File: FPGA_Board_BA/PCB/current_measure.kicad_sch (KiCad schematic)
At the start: 1 part, among them U2 AMC0300D

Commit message: some changes + lib
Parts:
- added U3, U6: AMC0300D, MYLIB_Misc:SOIC-8_7.5x5.85mm_P1.27mm, symbol MYLIB_U:AMC0300D
- U2: footprint Package_SO:SOIC-8_7.5x5.85mm_P1.27mm -> MYLIB_Misc:SOIC-8_7.5x5.85mm_P1.27mm
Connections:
- net Ph_A+: now also U6.2 (VIN+)
- net Ph_A-: now also U6.3 (VIN-)
- net Ph_B+: now also U2.2 (VIN+)
- net Ph_B-: now also U2.3 (VIN-)
- net Ph_C+: now also U3.2 (VIN+)
- net Ph_C-: now also U3.3 (VIN-)

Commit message: adding DCCD
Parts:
- removed U2, U3, U6: AMC0300D, MYLIB_Misc:SOIC-8_7.5x5.85mm_P1.27mm, symbol MYLIB_U:AMC0300D
- added U401, U402, U403: AMC0300D, MYLIB_Misc:SOIC-8_7.5x5.85mm_P1.27mm, symbol MYLIB_Misc:AMC0300D
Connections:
- net Ph_A+: now also U401.2 (VIN+)
- net Ph_A-: now also U401.3 (VIN-)
- net Ph_B+: now also U402.2 (VIN+)
- net Ph_B-: now also U402.3 (VIN-)
- net Ph_C+: now also U403.2 (VIN+)
- net Ph_C-: now also U403.3 (VIN-)
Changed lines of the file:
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@@
 	)
 	(symbol
-		(lib_name "AMC0300D_1")
-		(lib_id "MYLIB_U:AMC0300D")
+		(lib_id "MYLIB_Misc:AMC0300D")
 		(at 133.35 59.69 0)
 		(mirror y)
@@
 		(on_board yes)
 		(dnp no)
-		(property "Reference" "U6"
+		(fields_autoplaced yes)
+		(property "Reference" "U401"
 			(at 133.35 44.45 0)
 			(effects
@@
 		)
 		(property "Footprint" "MYLIB_Misc:SOIC-8_7.5x5.85mm_P1.27mm"
-			(at 132.588 32.766 0)
+			(at 133.604 35.306 0)
 			(effects
 				(font
@@
 		)
 		(property "Datasheet" "https://www.ti.com/lit/ds/symlink/amc0300d.pdf?ts=1761549500748&ref_url=https%253A%252F%252Fwww.ti.com%252Fproduct%252FAMC0300D%253FkeyMatch%253DAMC0300D%2526tisearch%253Duniversal_search%2526usecase%253DGPN"
-			(at 138.938 27.686 0)
-			(effects
-				(font
-					(size 1.27 1.27)
-				)
-				(hide yes)
-			)
-		)
-		(property "Description" "Isolation amplifier"
-			(at 134.112 29.972 0)
+			(at 132.842 37.846 0)
+			(effects
+				(font
+					(size 1.27 1.27)
+				)
+				(hide yes)
+			)
+		)
+		(property "Description" "isolation Amplifier"
+			(at 132.334 40.132 0)
 			(effects
 				(font
@@
 		(pin "3"
 		)
+		(pin "5"
+		)
+		(pin "1"
+		)
+		(pin "2"
+		)
+		(pin "7"
+		)
 		(pin "8"
 		)
-		(pin "1"
-		)
 		(pin "6"
-		)
-		(pin "5"
-		)
-		(pin "7"
-		)
-		(pin "2"
 		)
 		(instances
 			(project ""
 				(path "/fd7503bc-e7fc-4766-b224-3d1c3d7de5ff/6c3bdaeb-3a48-483c-8f1c-d2943b7053f6"
-					(reference "U6")
+					(reference "U401")
 					(unit 1)
 				)
@@
 	)
 	(symbol
-		(lib_name "AMC0300D_1")
-		(lib_id "MYLIB_U:AMC0300D")
+		(lib_id "MYLIB_Misc:AMC0300D")
+		(at 133.35 97.79 0)
+		(mirror y)
+		(unit 1)
+		(exclude_from_sim no)
+		(in_bom yes)
+		(on_board yes)
+		(dnp no)
+		(fields_autoplaced yes)
+		(property "Reference" "U402"
+			(at 133.35 82.55 0)
+			(effects
+				(font
+					(size 1.27 1.27)
+				)
+			)
+		)
+		(property "Value" "AMC0300D"
+			(at 133.35 85.09 0)
+			(effects
+				(font
+					(size 1.27 1.27)
+				)
+			)
+		)
+		(property "Footprint" "MYLIB_Misc:SOIC-8_7.5x5.85mm_P1.27mm"
+			(at 133.604 73.406 0)
+			(effects
+				(font
+					(size 1.27 1.27)
+				)
+				(hide yes)
+			)
+		)
+		(property "Datasheet" "https://www.ti.com/lit/ds/symlink/amc0300d.pdf?ts=1761549500748&ref_url=https%253A%252F%252Fwww.ti.com%252Fproduct%252FAMC0300D%253FkeyMatch%253DAMC0300D%2526tisearch%253Duniversal_search%2526usecase%253DGPN"
+			(at 132.842 75.946 0)
+			(effects
+				(font
+					(size 1.27 1.27)
+				)
+				(hide yes)
+			)
+		)
+		(property "Description" "isolation Amplifier"
+			(at 132.334 78.232 0)
+			(effects
+				(font
+					(size 1.27 1.27)
+				)
+				(hide yes)
+			)
+		)
+		(pin "4"
+		)
+		(pin "3"
+		)
+		(pin "5"
+		)
+		(pin "1"
+		)
+		(pin "2"
+		)
+		(pin "7"
+		)
+		(pin "8"
+		)
+		(pin "6"
+		)
+		(instances
+			(project "FPGA_Board_BA"
+				(path "/fd7503bc-e7fc-4766-b224-3d1c3d7de5ff/6c3bdaeb-3a48-483c-8f1c-d2943b7053f6"
+					(reference "U402")
+					(unit 1)
+				)
+			)
+		)
+	)
+	(symbol
+		(lib_id "MYLIB_Misc:AMC0300D")
 		(at 134.62 137.16 0)
 		(mirror y)
@@
 		(on_board yes)
 		(dnp no)
-		(property "Reference" "U3"
+		(fields_autoplaced yes)
+		(property "Reference" "U403"
 			(at 134.62 121.92 0)
 			(effects
@@
 		)
 		(property "Footprint" "MYLIB_Misc:SOIC-8_7.5x5.85mm_P1.27mm"
-			(at 133.858 110.236 0)
+			(at 134.874 112.776 0)
 			(effects
 				(font
@@
 		)
 		(property "Datasheet" "https://www.ti.com/lit/ds/symlink/amc0300d.pdf?ts=1761549500748&ref_url=https%253A%252F%252Fwww.ti.com%252Fproduct%252FAMC0300D%253FkeyMatch%253DAMC0300D%2526tisearch%253Duniversal_search%2526usecase%253DGPN"
-			(at 140.208 105.156 0)
-			(effects
-				(font
-					(size 1.27 1.27)
-				)
-				(hide yes)
-			)
-		)
-		(property "Description" "Isolation amplifier"
-			(at 135.382 107.442 0)
+			(at 134.112 115.316 0)
+			(effects
+				(font
+					(size 1.27 1.27)
+				)
+				(hide yes)
+			)
+		)
+		(property "Description" "isolation Amplifier"
+			(at 133.604 117.602 0)
 			(effects
 				(font
@@
 		(pin "3"
 		)
+		(pin "5"
+		)
+		(pin "1"
+		)
+		(pin "2"
+		)
+		(pin "7"
+		)
 		(pin "8"
 		)
-		(pin "1"
-		)
 		(pin "6"
-		)
-		(pin "5"
-		)
-		(pin "7"
-		)
-		(pin "2"
 		)
 		(instances
 			(project "FPGA_Board_BA"
 				(path "/fd7503bc-e7fc-4766-b224-3d1c3d7de5ff/6c3bdaeb-3a48-483c-8f1c-d2943b7053f6"
-					(reference "U3")
+					(reference "U403")
 					(unit 1)
 				)
-			)
-		)
-	)
-	(symbol
-		(lib_name "AMC0300D_1")
-		(lib_id "MYLIB_U:AMC0300D")
-		(at 133.35 97.79 0)
-		(mirror y)
-		(unit 1)
-		(exclude_from_sim no)
-		(in_bom yes)
-		(on_board yes)
-		(dnp no)
-		(property "Reference" "U2"
-			(at 133.35 82.55 0)
-			(effects
-				(font
-					(size 1.27 1.27)
-				)
-			)
-		)
-		(property "Value" "AMC0300D"
-			(at 133.35 85.09 0)
-			(effects
-				(font
-					(size 1.27 1.27)
-				)
-			)
-		)
-		(property "Footprint" "MYLIB_Misc:SOIC-8_7.5x5.85mm_P1.27mm"
-			(at 132.588 70.866 0)
-			(effects
-				(font
-					(size 1.27 1.27)
-				)
-				(hide yes)
-			)
-		)
-		(property "Datasheet" "https://www.ti.com/lit/ds/symlink/amc0300d.pdf?ts=1761549500748&ref_url=https%253A%252F%252Fwww.ti.com%252Fproduct%252FAMC0300D%253FkeyMatch%253DAMC0300D%2526tisearch%253Duniversal_search%2526usecase%253DGPN"
-			(at 138.938 65.786 0)
-			(effects
-				(font
-					(size 1.27 1.27)
-				)
-				(hide yes)
-			)
-		)
-		(property "Description" "Isolation amplifier"
-			(at 134.112 68.072 0)
-			(effects
-				(font
-					(size 1.27 1.27)
-				)
-				(hide yes)
-			)
-		)
-		(pin "4"
-		)
-		(pin "3"
-		)
-		(pin "8"
-		)
-		(pin "1"
-		)
-		(pin "6"
-		)
-		(pin "5"
-		)
-		(pin "7"
-		)
-		(pin "2"
-		)
-		(instances
-			(project "FPGA_Board_BA"
-				(path "/fd7503bc-e7fc-4766-b224-3d1c3d7de5ff/6c3bdaeb-3a48-483c-8f1c-d2943b7053f6"
-					(reference "U2")
-					(unit 1)
-				)

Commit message: schematic almost ready
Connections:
- net PHA_OUTN: now reaches U401.6 (VOUT-)
- net PHA_OUTP: now reaches U401.7 (VOUT+)
- net PHB_OUTN: now reaches U402.6 (VOUT-)
- net PHB_OUTP: now reaches U402.7 (VOUT+)
- net PHC_OUTN: now reaches U403.6 (VOUT-)
- net PHC_OUTP: now reaches U403.7 (VOUT+)
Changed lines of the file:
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@@
+	(wire
+		(pts
+			(xy 106.68 62.23) (xy 118.11 62.23)
+		)
+		(stroke
+			(width 0)
+			(type default)
+		)
+	)
 	(wire
 		(pts
@@
 	(wire
 		(pts
+			(xy 106.68 100.33) (xy 118.11 100.33)
+		)
+		(stroke
+			(width 0)
+			(type default)
+		)
+	)
+	(wire
+		(pts
 			(xy 148.59 95.25) (xy 154.94 95.25)
 		)
@@
 	(wire
 		(pts
+			(xy 107.95 139.7) (xy 119.38 139.7)
+		)
+		(stroke
+			(width 0)
+			(type default)
+		)
+	)
+	(wire
+		(pts
 			(xy 149.86 134.62) (xy 156.21 134.62)
 		)
@@
 	(wire
 		(pts
+			(xy 107.95 134.62) (xy 119.38 134.62)
+		)
+		(stroke
+			(width 0)
+			(type default)
+		)
+	)
+	(wire
+		(pts
 			(xy 148.59 57.15) (xy 157.48 57.15)
 		)
@@
 		)
 	)
+	(wire
+		(pts
+			(xy 106.68 95.25) (xy 118.11 95.25)
+		)
+		(stroke
+			(width 0)
+			(type default)
+		)
+	)
+	(wire
+		(pts
+			(xy 106.68 57.15) (xy 118.11 57.15)
+		)
+		(stroke
+			(width 0)
+			(type default)
+		)
+	)
 	(hierarchical_label "Ph_C-"
 		(shape input)
@@
 		)
 	)
+	(hierarchical_label "PHC_OUTN"
+		(shape output)
+		(at 107.95 139.7 180)
+		(effects
+			(font
+				(size 1.27 1.27)
+			)
+			(justify right)
+		)
+	)
 	(hierarchical_label "Ph_B+"
 		(shape input)
@@
 		)
 	)
+	(hierarchical_label "PHA_OUTN"
+		(shape output)
+		(at 106.68 62.23 180)
+		(effects
+			(font
+				(size 1.27 1.27)
+			)
+			(justify right)
+		)
+	)
 	(hierarchical_label "Ph_A+"
 		(shape input)
@@
 		)
 	)
+	(hierarchical_label "PHB_OUTP"
+		(shape output)
+		(at 106.68 95.25 180)
+		(effects
+			(font
+				(size 1.27 1.27)
+			)
+			(justify right)
+		)
+	)
+	(hierarchical_label "PHA_OUTP"
+		(shape output)
+		(at 106.68 57.15 180)
+		(effects
+			(font
+				(size 1.27 1.27)
+			)
+			(justify right)
+		)
+	)
+	(hierarchical_label "PHC_OUTP"
+		(shape output)
+		(at 107.95 134.62 180)
+		(effects
+			(font
+				(size 1.27 1.27)
+			)
+			(justify right)
+		)
+	)
+	(hierarchical_label "PHB_OUTN"
+		(shape output)
+		(at 106.68 100.33 180)
+		(effects
+			(font
+				(size 1.27 1.27)
+			)
+			(justify right)
+		)
+	)

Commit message: some schematic changes + Misc
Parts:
- added U404: AMC0300D, MYLIB_Misc:SOIC-8_7.5x5.85mm_P1.27mm, symbol MYLIB_Misc:AMC0300D
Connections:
- new net PHD_OUTN: U404.6 (VOUT-)
- new net PHD_OUTP: U404.7 (VOUT+)
- new net Ph_D+: U404.2 (VIN+)
- new net Ph_D-: U404.3 (VIN-)
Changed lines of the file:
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@@
+	(wire
+		(pts
+			(xy 107.95 173.99) (xy 119.38 173.99)
+		)
+		(stroke
+			(width 0)
+			(type default)
+		)
+	)
 	(wire
 		(pts
@@
 	(wire
 		(pts
+			(xy 107.95 179.07) (xy 119.38 179.07)
+		)
+		(stroke
+			(width 0)
+			(type default)
+		)
+	)
+	(wire
+		(pts
+			(xy 149.86 173.99) (xy 156.21 173.99)
+		)
+		(stroke
+			(width 0)
+			(type default)
+		)
+	)
+	(wire
+		(pts
 			(xy 148.59 57.15) (xy 157.48 57.15)
 		)
@@
 	(wire
 		(pts
+			(xy 149.86 179.07) (xy 156.21 179.07)
+		)
+		(stroke
+			(width 0)
+			(type default)
+		)
+	)
+	(wire
+		(pts
 			(xy 148.59 62.23) (xy 157.48 62.23)
 		)
@@
 		)
 	)
+	(hierarchical_label "Ph_D+"
+		(shape input)
+		(at 156.21 173.99 0)
+		(effects
+			(font
+				(size 1.27 1.27)
+			)
+			(justify left)
+		)
+	)
 	(hierarchical_label "Ph_B+"
 		(shape input)
@@
 		)
 	)
+	(hierarchical_label "PHD_OUTP"
+		(shape output)
+		(at 107.95 173.99 180)
+		(effects
+			(font
+				(size 1.27 1.27)
+			)
+			(justify right)
+		)
+	)
 	(hierarchical_label "PHB_OUTP"
 		(shape output)
@@
 			)
 			(justify right)
+		)
+	)
+	(hierarchical_label "PHD_OUTN"
+		(shape output)
+		(at 107.95 179.07 180)
+		(effects
+			(font
+				(size 1.27 1.27)
+			)
+			(justify right)
+		)
+	)
+	(hierarchical_label "Ph_D-"
+		(shape input)
+		(at 156.21 179.07 0)
+		(effects
+			(font
+				(size 1.27 1.27)
+			)
+			(justify left)
 		)
 	)
@@
 					(unit 1)
 				)
+			)
+		)
+	)
+	(symbol
+		(lib_id "MYLIB_Misc:AMC0300D")
+		(at 134.62 176.53 0)
+		(mirror y)
+		(unit 1)
+		(exclude_from_sim no)
+		(in_bom yes)
+		(on_board yes)
+		(dnp no)
+		(fields_autoplaced yes)
+		(property "Reference" "U404"
+			(at 134.62 161.29 0)
+			(effects
+				(font
+					(size 1.27 1.27)
+				)
+			)
+		)
+		(property "Value" "AMC0300D"
+			(at 134.62 163.83 0)
+			(effects
+				(font
+					(size 1.27 1.27)
+				)
+			)
+		)
+		(property "Footprint" "MYLIB_Misc:SOIC-8_7.5x5.85mm_P1.27mm"
+			(at 134.874 152.146 0)
+			(effects
+				(font
+					(size 1.27 1.27)
+				)
+				(hide yes)
+			)
+		)
+		(property "Datasheet" "https://www.ti.com/lit/ds/symlink/amc0300d.pdf?ts=1761549500748&ref_url=https%253A%252F%252Fwww.ti.com%252Fproduct%252FAMC0300D%253FkeyMatch%253DAMC0300D%2526tisearch%253Duniversal_search%2526usecase%253DGPN"
+			(at 134.112 154.686 0)
+			(effects
+				(font
+					(size 1.27 1.27)
+				)
+				(hide yes)
+			)
+		)
+		(property "Description" "isolation Amplifier"
+			(at 133.604 156.972 0)
+			(effects
+				(font
+					(size 1.27 1.27)
+				)
+				(hide yes)
+			)
+		)
+		(pin "4"
+		)
+		(pin "3"
+		)
+		(pin "5"
+		)
+		(pin "1"
+		)
+		(pin "2"
+		)
+		(pin "7"
+		)
+		(pin "8"
+		)
+		(pin "6"
+		)
+		(instances
+			(project "FPGA_Board_BA"
+				(path "/fd7503bc-e7fc-4766-b224-3d1c3d7de5ff/6c3bdaeb-3a48-483c-8f1c-d2943b7053f6"
+					(reference "U404")
+					(unit 1)
+				)

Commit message: lot of work
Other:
- moved on the sheet: U401, U402, U403, U404

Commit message: work
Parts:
- renumbered U401 to U3, U402 to U4, U403 to U5, U404 to U6
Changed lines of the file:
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@@
 		(dnp no)
 		(fields_autoplaced yes)
-		(property "Reference" "U401"
+		(property "Reference" "U3"
 			(at 133.35 26.67 0)
 			(effects
@@
 			(project ""
 				(path "/fd7503bc-e7fc-4766-b224-3d1c3d7de5ff/6c3bdaeb-3a48-483c-8f1c-d2943b7053f6"
-					(reference "U401")
+					(reference "U3")
 					(unit 1)
 				)
@@
 		(dnp no)
 		(fields_autoplaced yes)
-		(property "Reference" "U404"
+		(property "Reference" "U6"
 			(at 134.62 143.51 0)
 			(effects
@@
 			(project "FPGA_Board_BA"
 				(path "/fd7503bc-e7fc-4766-b224-3d1c3d7de5ff/6c3bdaeb-3a48-483c-8f1c-d2943b7053f6"
-					(reference "U404")
+					(reference "U6")
 					(unit 1)
 				)
@@
 		(dnp no)
 		(fields_autoplaced yes)
-		(property "Reference" "U402"
+		(property "Reference" "U4"
 			(at 133.35 64.77 0)
 			(effects
@@
 			(project "FPGA_Board_BA"
 				(path "/fd7503bc-e7fc-4766-b224-3d1c3d7de5ff/6c3bdaeb-3a48-483c-8f1c-d2943b7053f6"
-					(reference "U402")
+					(reference "U4")
 					(unit 1)
 				)
@@
 		(dnp no)
 		(fields_autoplaced yes)
-		(property "Reference" "U403"
+		(property "Reference" "U5"
 			(at 134.62 104.14 0)
 			(effects
@@
 			(project "FPGA_Board_BA"
 				(path "/fd7503bc-e7fc-4766-b224-3d1c3d7de5ff/6c3bdaeb-3a48-483c-8f1c-d2943b7053f6"
-					(reference "U403")
+					(reference "U5")
 					(unit 1)
 				)

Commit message: 22.11
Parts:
- removed U3, U4, U5, U6: AMC0300D, MYLIB_Misc:SOIC-8_7.5x5.85mm_P1.27mm, symbol MYLIB_Misc:AMC0300D
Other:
- added sheet Tamura_1 (tamura.kicad_sch)
- added sheet Tamura_2 (tamura.kicad_sch)
- added sheet Tamura_3 (tamura.kicad_sch)
- added sheet Tamura_4 (tamura.kicad_sch)

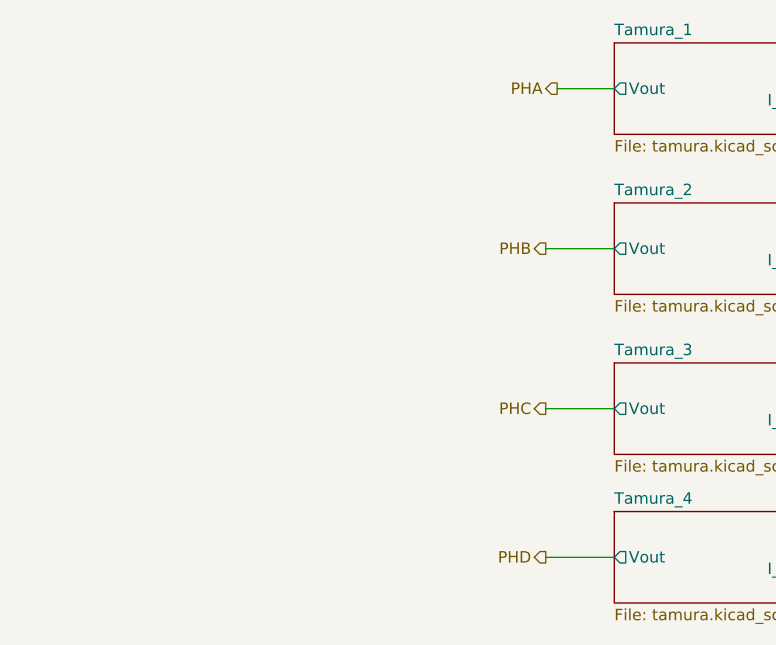
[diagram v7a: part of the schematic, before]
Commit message: big schematic cleanup. Added wire to bus
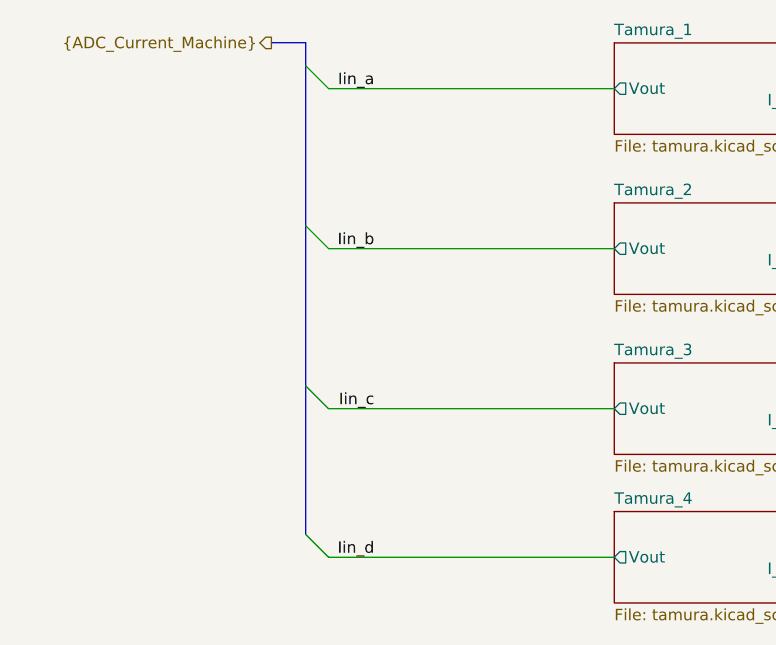
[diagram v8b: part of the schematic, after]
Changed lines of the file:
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@@
 	(generator_version "9.0")
 	(paper "A4")
+	(bus_entry
+		(at 74.93 93.98)
+		(size -2.54 -2.54)
+		(stroke
+			(width 0)
+			(type default)
+		)
+	)
+	(bus_entry
+		(at 74.93 110.49)
+		(size -2.54 -2.54)
+		(stroke
+			(width 0)
+			(type default)
+		)
+	)
+	(bus_entry
+		(at 74.93 58.42)
+		(size -2.54 -2.54)
+		(stroke
+			(width 0)
+			(type default)
+		)
+	)
+	(bus_entry
+		(at 74.93 76.2)
+		(size -2.54 -2.54)
+		(stroke
+			(width 0)
+			(type default)
+		)
+	)
 	(wire
 		(pts
@@
 		)
 	)
-	(wire
-		(pts
-			(xy 99.06 110.49) (xy 106.68 110.49)
+	(bus
+		(pts
+			(xy 72.39 55.88) (xy 72.39 53.34)
 		)
 		(stroke
@@
 	(wire
 		(pts
-			(xy 100.33 58.42) (xy 106.68 58.42)
+			(xy 74.93 93.98) (xy 106.68 93.98)
+		)
+		(stroke
+			(width 0)
+			(type default)
+		)
+	)
+	(bus
+		(pts
+			(xy 72.39 73.66) (xy 72.39 55.88)
+		)
+		(stroke
+			(width 0)
+			(type default)
+		)
+	)
+	(bus
+		(pts
+			(xy 72.39 91.44) (xy 72.39 73.66)
 		)
 		(stroke
@@
 		)
 	)
+	(bus
+		(pts
+			(xy 72.39 107.95) (xy 72.39 91.44)
+		)
+		(stroke
+			(width 0)
+			(type default)
+		)
+	)
+	(wire
+		(pts
+			(xy 74.93 76.2) (xy 106.68 76.2)
+		)
+		(stroke
+			(width 0)
+			(type default)
+		)
+	)
+	(wire
+		(pts
+			(xy 74.93 110.49) (xy 106.68 110.49)
+		)
+		(stroke
+			(width 0)
+			(type default)
+		)
+	)
 	(wire
 		(pts
@@
 		)
 	)
-	(wire
-		(pts
-			(xy 99.06 93.98) (xy 106.68 93.98)
+	(bus
+		(pts
+			(xy 72.39 53.34) (xy 68.58 53.34)
 		)
 		(stroke
@@
 	(wire
 		(pts
+			(xy 74.93 58.42) (xy 106.68 58.42)
+		)
+		(stroke
+			(width 0)
+			(type default)
+		)
+	)
+	(wire
+		(pts
 			(xy 129.54 111.76) (xy 134.62 111.76)
 		)
@@
 		)
 	)
-	(wire
-		(pts
-			(xy 99.06 76.2) (xy 106.68 76.2)
-		)
-		(stroke
-			(width 0)
-			(type default)
+	(label "Iin_a"
+		(at 80.01 58.42 180)
+		(effects
+			(font
+				(size 1.27 1.27)
+			)
+			(justify right bottom)
+		)
+	)
+	(label "Iin_b"
+		(at 80.01 76.2 180)
+		(effects
+			(font
+				(size 1.27 1.27)
+			)
+			(justify right bottom)
+		)
+	)
+	(label "Iin_d"
+		(at 80.01 110.49 180)
+		(effects
+			(font
+				(size 1.27 1.27)
+			)
+			(justify right bottom)
+		)
+	)
+	(label "Iin_c"
+		(at 80.01 93.98 180)
+		(effects
+			(font
+				(size 1.27 1.27)
+			)
+			(justify right bottom)
 		)
 	)
@@
 		)
 	)
+	(hierarchical_label "{ADC_Current_Machine}"
+		(shape output)
+		(at 68.58 53.34 180)
+		(effects
+			(font
+				(size 1.27 1.27)
+			)
+			(justify right)
+		)
+	)
 	(hierarchical_label "Ph_D+"
 		(shape input)
@@
 		)
 	)
-	(hierarchical_label "PHD"
-		(shape output)
-		(at 99.06 110.49 180)
-		(effects
-			(font
-				(size 1.27 1.27)
-			)
-			(justify right)
-		)
-	)
-	(hierarchical_label "PHB"
-		(shape output)
-		(at 99.06 76.2 180)
-		(effects
-			(font
-				(size 1.27 1.27)
-			)
-			(justify right)
-		)
-	)
 	(hierarchical_label "Ph_D-"
 		(shape input)
@@
 		)
 	)
-	(hierarchical_label "PHA"
-		(shape output)
-		(at 100.33 58.42 180)
-		(effects
-			(font
-				(size 1.27 1.27)
-			)
-			(justify right)
-		)
-	)
-	(hierarchical_label "PHC"
-		(shape output)
-		(at 99.06 93.98 180)
-		(effects
-			(font
-				(size 1.27 1.27)
-			)
-			(justify right)
-		)
-	)
